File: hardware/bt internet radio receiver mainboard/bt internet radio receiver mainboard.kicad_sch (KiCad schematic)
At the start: 54 parts, among them J1 +5V_in, J10 I2C, J11 Conn_01x05_Socket, J12 Conn_01x02_Socket, J13 Conn_01x08_Socket, J14 Conn_01x05_Socket, J15 ESP_1_UART, J16 IR_REM, J17 Conn_01x02_Socket, J2 Mode_sw_in, J3 Audio_sw_out, J4 VFD_conn, J5 Enc_conn, J6 Btn_conn, J7 PCM5102A input conn, J8 PCM5102A ctrl/out conn, J9 Analog out, U1 ESP32-DevKitC, U2 ESP32-DevKitC, U3 74LS157, U4 M24C02-RMN

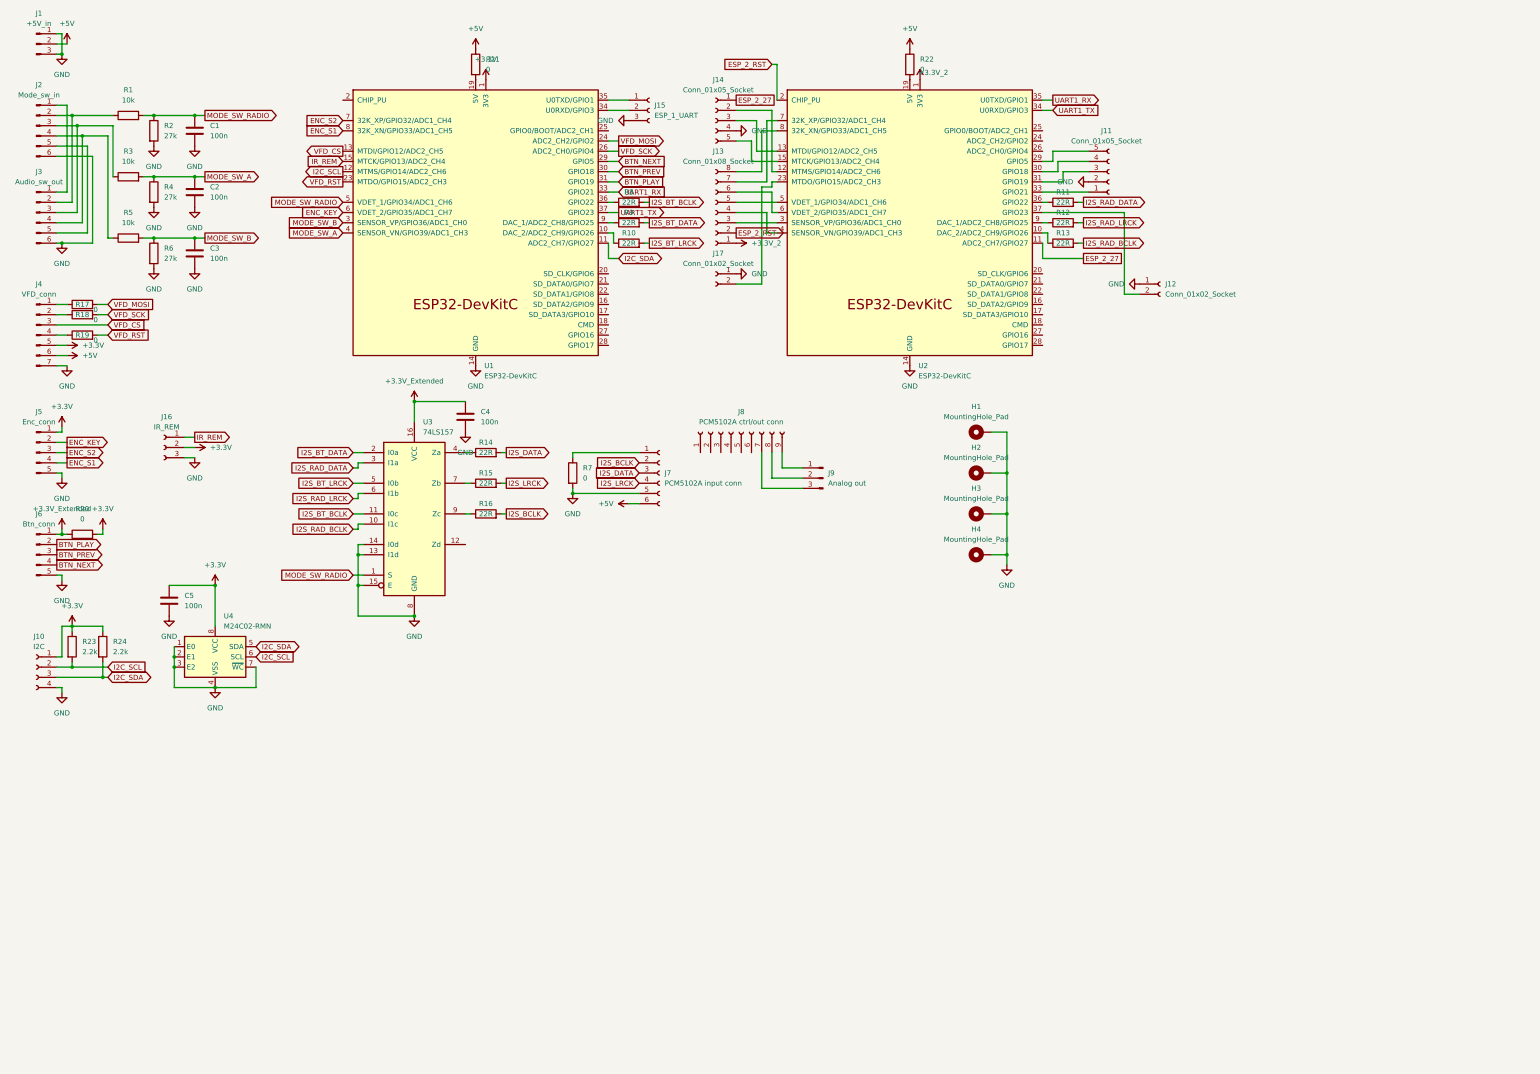
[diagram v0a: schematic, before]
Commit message: Cosmetic cleanup in schematics, add schematic PDF exports
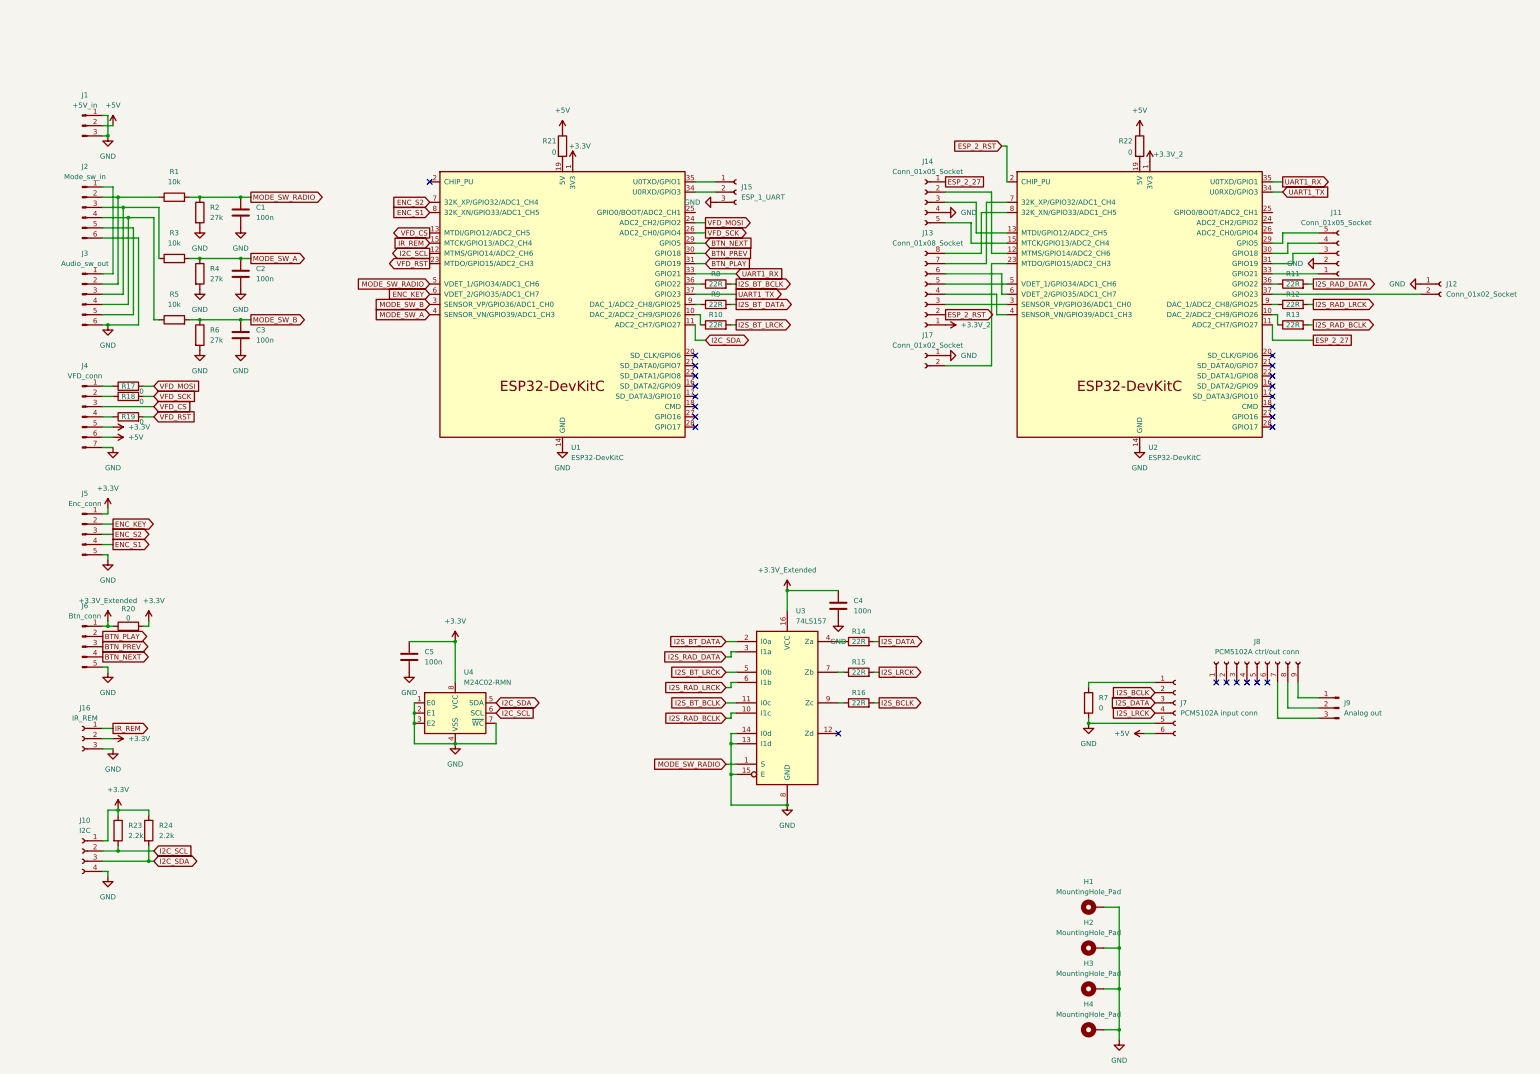
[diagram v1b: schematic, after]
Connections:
- no-connect marks 0 -> 24
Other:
- title: (none) -> Audiostreamer Mainboard
- moved on the sheet: C1, C2, C3, C4, C5, H1, H2, H3, H4, J1, J10, J11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
